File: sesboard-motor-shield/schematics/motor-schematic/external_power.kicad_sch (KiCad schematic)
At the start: 9 parts, among them J1 12Vin(MAX), Q1 Q_NMOS_DGS, Q2 TIP3055, U1 LM317_SOT-223

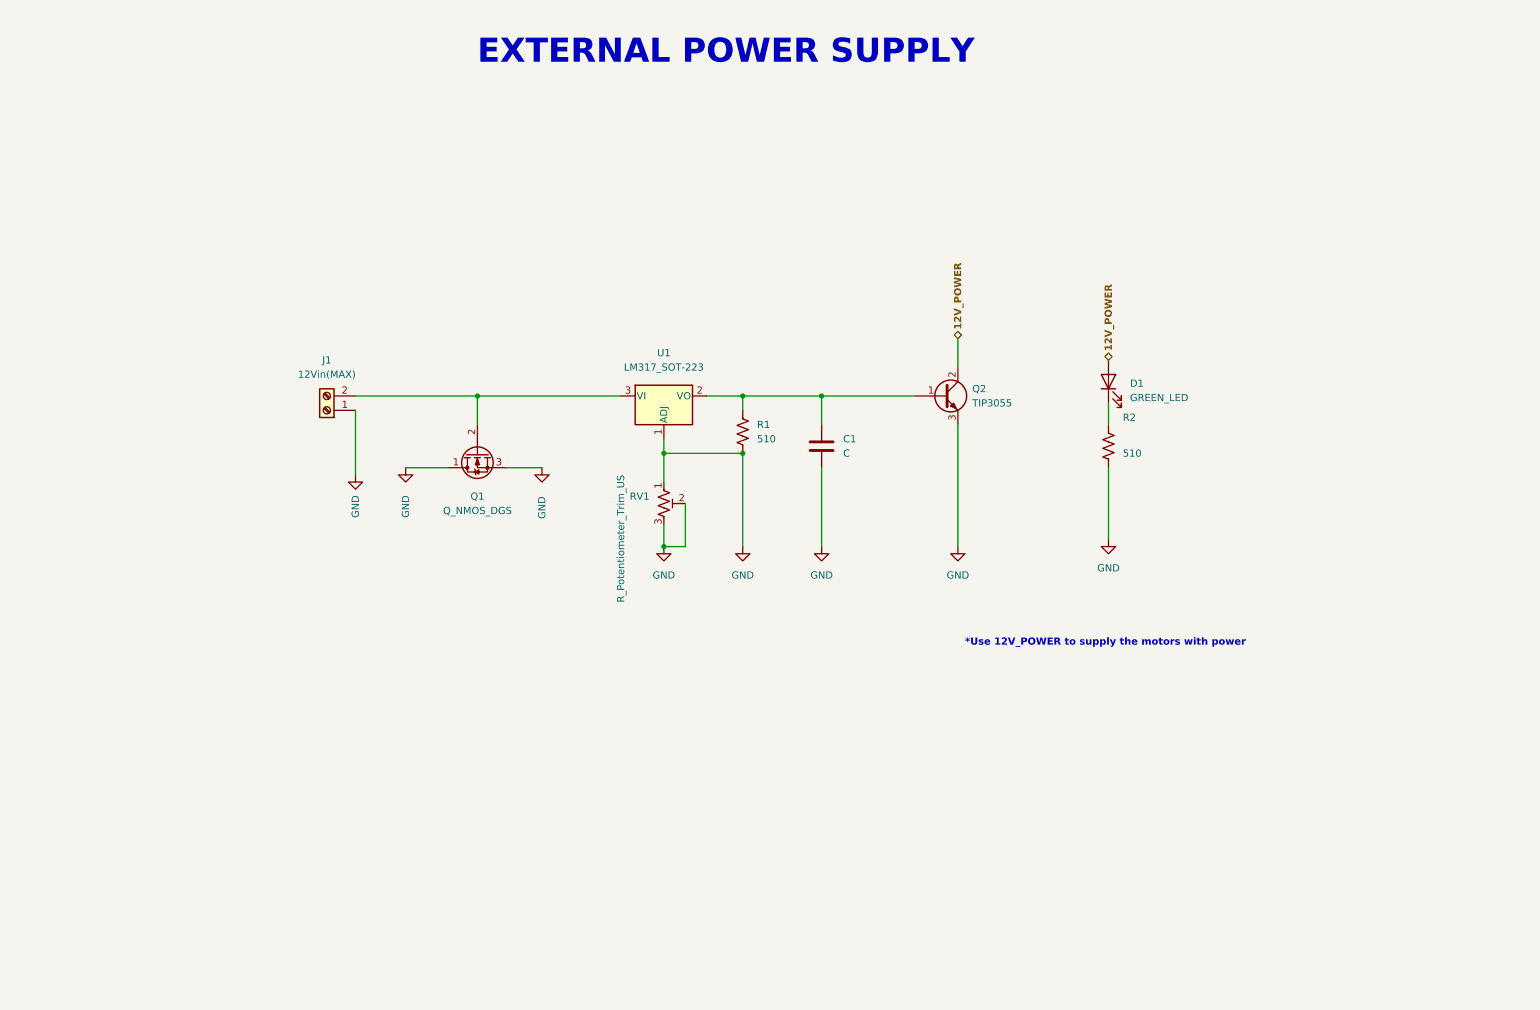
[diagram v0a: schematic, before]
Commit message: added servo power supply
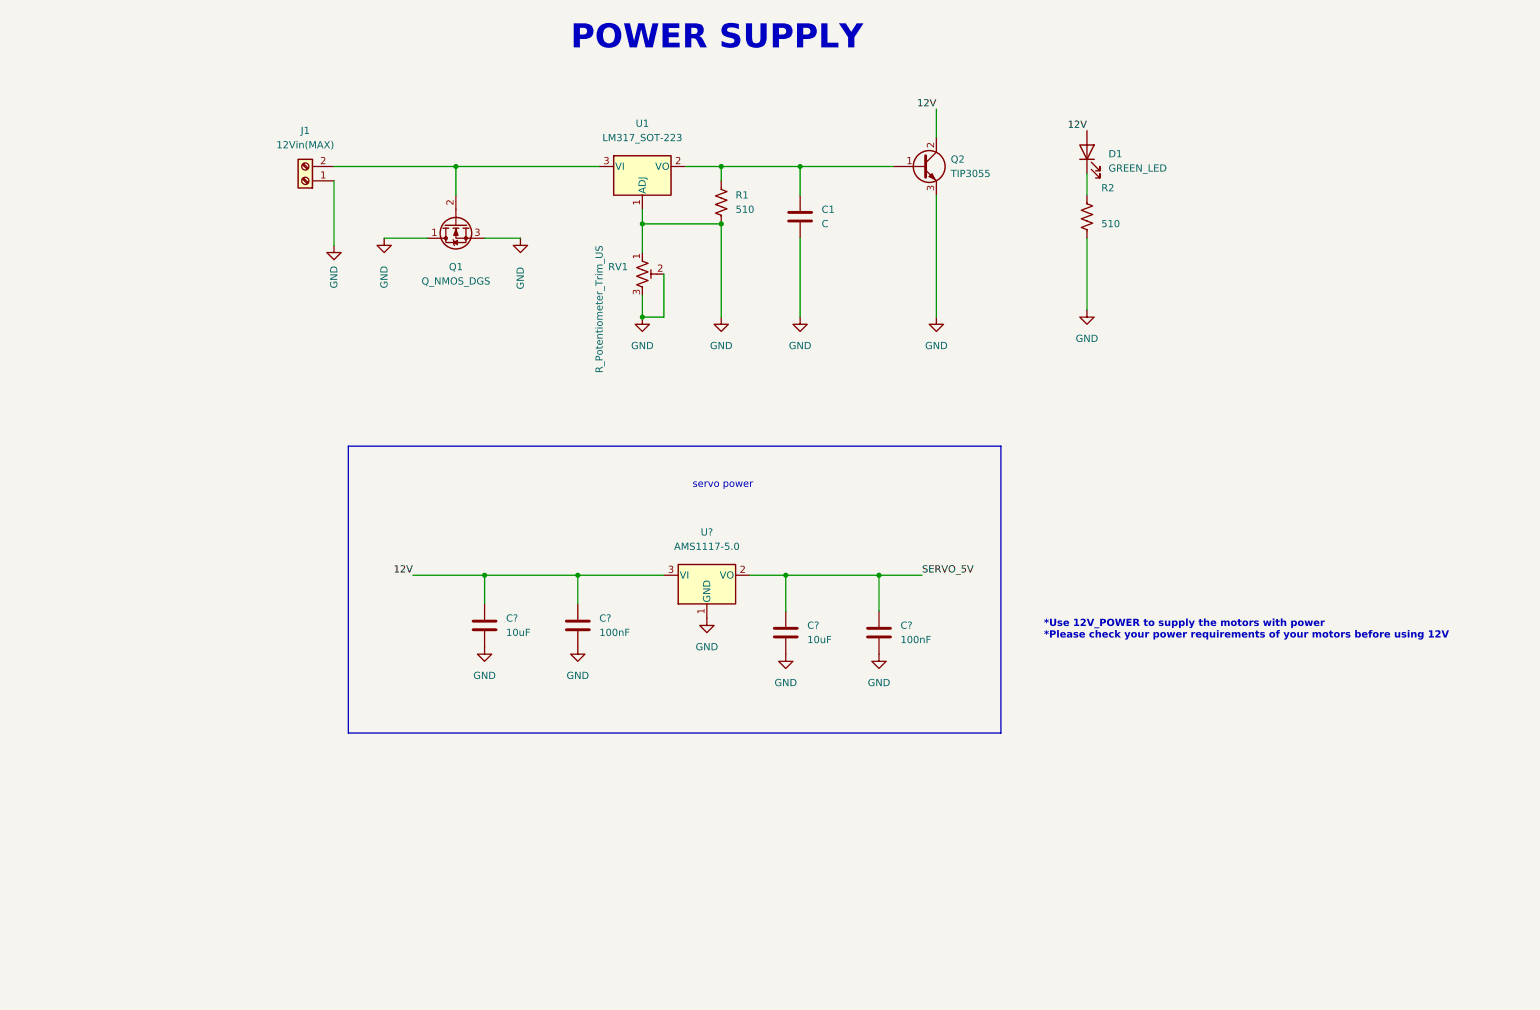
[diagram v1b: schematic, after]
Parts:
- added C? (x2): 10uF, symbol Device:C
- added C? (x2): 100nF, symbol Device:C
- added U?: AMS1117-5.0, Package_TO_SOT_SMD:SOT-223-3_TabPin2, symbol Regulator_Linear:AMS1117-5.0
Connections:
- net GND: now also C?.2, C?.2, C?.2, C?.2, U?.1 (GND)
- net 12V_POWER renamed 12V
- net 12V: now also C?.1, C?.1, U?.3 (VI)
- new net SERVO_5V: C?.1, C?.1, U?.2 (VO)
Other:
- note added: "*Use 12V_POWER to supply the motors with power *Please check your power requirements of your motors before using 12V"
- note added: "POWER SUPPLY"
- note added: "servo power"
- note removed: "*Use 12V_POWER to supply the motors with power"
- note removed: "EXTERNAL POWER SUPPLY"
- moved on the sheet: C1, D1, J1, Q1, Q2, R1, R2, RV1, U1

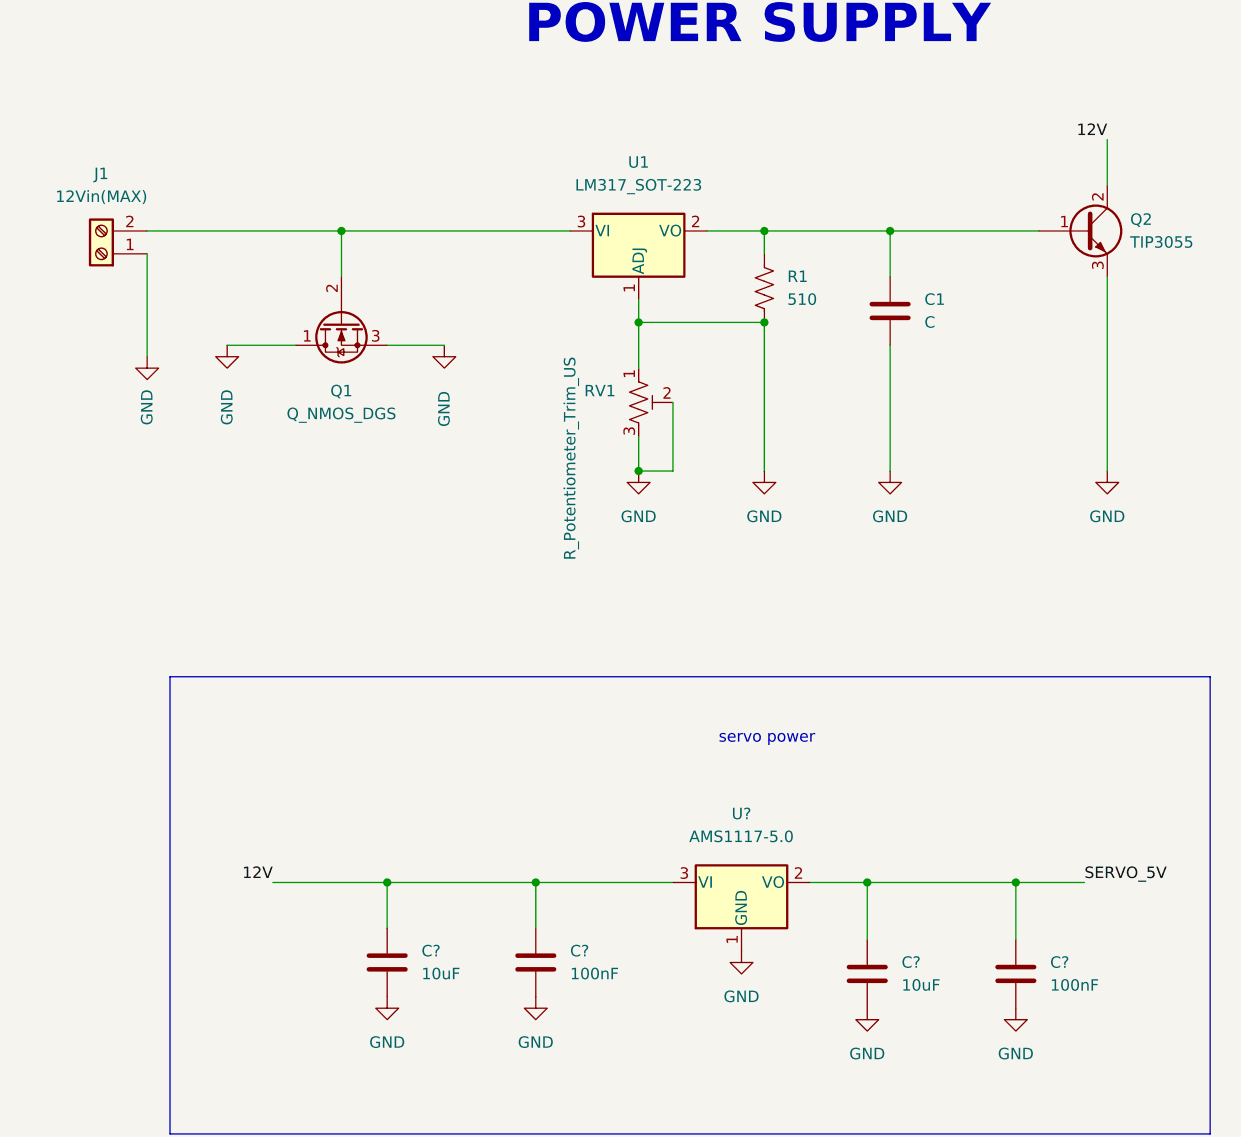
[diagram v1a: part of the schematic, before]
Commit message: performed ERC
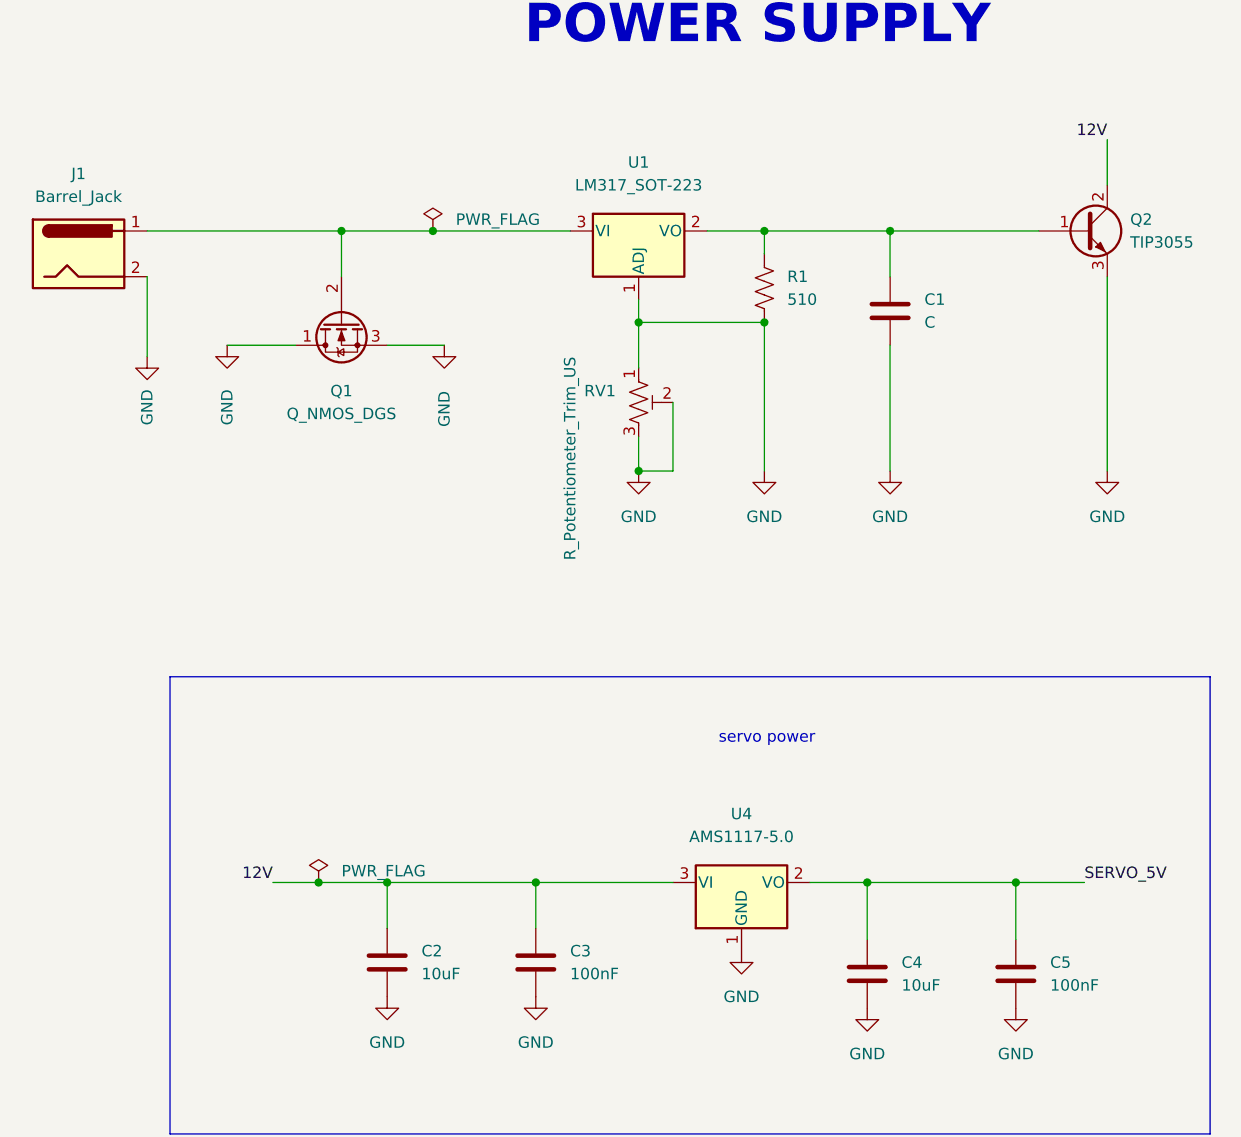
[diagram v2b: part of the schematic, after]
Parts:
- removed J1: 12Vin(MAX), symbol Connector:Screw_Terminal_01x02
- added J1: Barrel_Jack, symbol Connector:Barrel_Jack
- gave numbers to parts that had none: 5
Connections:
- net GND: now also J1.2
- net at Q1.2 (G), U1.3 (VI): now also J1.1
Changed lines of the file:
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@@
   (junction (at 160.02 41.91) (diameter 0) (color 0 0 0 0)
   )
+  (junction (at 96.52 114.3) (diameter 0) (color 0 0 0 0)
+  )
   (junction (at 99.06 41.91) (diameter 0) (color 0 0 0 0)
   )
   (junction (at 146.05 52.07) (diameter 0) (color 0 0 0 0)
   )
+  (junction (at 109.22 41.91) (diameter 0) (color 0 0 0 0)
+  )
   (junction (at 132.08 68.58) (diameter 0) (color 0 0 0 0)
   )
@@
     (stroke (width 0) (type default) (color 0 0 0 0))
   )
-  (wire (pts (xy 99.06 41.91) (xy 124.46 41.91))
+  (wire (pts (xy 99.06 41.91) (xy 109.22 41.91))
     (stroke (width 0) (type default) (color 0 0 0 0))
   )
@@
     (stroke (width 0) (type default) (color 0 0 0 0))
   )
-  (wire (pts (xy 77.47 55.88) (xy 77.47 44.45))
+  (wire (pts (xy 77.47 55.88) (xy 77.47 46.99))
     (stroke (width 0) (type default) (color 0 0 0 0))
   )
@@
     (stroke (width 0) (type default) (color 0 0 0 0))
   )
+  (wire (pts (xy 96.52 114.3) (xy 104.14 114.3))
+    (stroke (width 0) (type default) (color 0 0 0 0))
+  )
   (wire (pts (xy 146.05 41.91) (xy 139.7 41.91))
     (stroke (width 0) (type default) (color 0 0 0 0))
@@
     (stroke (width 0) (type default) (color 0 0 0 0))
   )
+  (wire (pts (xy 109.22 41.91) (xy 124.46 41.91))
+    (stroke (width 0) (type default) (color 0 0 0 0))
+  )
   (wire (pts (xy 210.82 43.18) (xy 210.82 46.99))
     (stroke (width 0) (type default) (color 0 0 0 0))
@@
     (stroke (width 0) (type default) (color 0 0 0 0))
   )
-  (wire (pts (xy 91.44 114.3) (xy 104.14 114.3))
+  (wire (pts (xy 91.44 114.3) (xy 96.52 114.3))
     (stroke (width 0) (type default) (color 0 0 0 0))
   )
@@
     (pin "2")
   )
+  (symbol (lib_id "power:PWR_FLAG") (at 109.22 41.91 0) (unit 1)
+    (in_bom yes) (on_board yes) (fields_autoplaced)
+    (property "Reference" "#FLG0101" (id 0) (at 109.22 40.005 0)
+      (effects (font (size 1.27 1.27)) hide)
+    )
+    (property "Value" "PWR_FLAG" (id 1) (at 111.76 40.6399 0)
+      (effects (font (size 1.27 1.27)) (justify left))
+    )
+    (property "Footprint" "" (id 2) (at 109.22 41.91 0)
+      (effects (font (size 1.27 1.27)) hide)
+    )
+    (property "Datasheet" "~" (id 3) (at 109.22 41.91 0)
+      (effects (font (size 1.27 1.27)) hide)
+    )
+    (pin "1")
+  )
   (symbol (lib_id "Device:C") (at 157.48 124.46 0) (unit 1)
     (in_bom yes) (on_board yes) (fields_autoplaced)
-    (property "Reference" "C?" (id 0) (at 161.29 123.1899 0)
+    (property "Reference" "C4" (id 0) (at 161.29 123.1899 0)
       (effects (font (size 1.27 1.27)) (justify left))
     )
@@
   (symbol (lib_id "Device:C") (at 173.99 124.46 0) (unit 1)
     (in_bom yes) (on_board yes)
-    (property "Reference" "C?" (id 0) (at 177.8 123.1899 0)
+    (property "Reference" "C5" (id 0) (at 177.8 123.1899 0)
       (effects (font (size 1.27 1.27)) (justify left))
     )
@@
   (symbol (lib_id "Regulator_Linear:AMS1117-5.0") (at 143.51 114.3 0) (unit 1)
     (in_bom yes) (on_board yes) (fields_autoplaced)
-    (property "Reference" "U?" (id 0) (at 143.51 106.68 0))
+    (property "Reference" "U4" (id 0) (at 143.51 106.68 0))
     (property "Value" "AMS1117-5.0" (id 1) (at 143.51 109.22 0))
     (property "Footprint" "Package_TO_SOT_SMD:SOT-223-3_TabPin2" (id 2) (at 143.51 109.22 0)
@@
     (pin "1")
   )
-  (symbol (lib_id "Connector:Screw_Terminal_01x02") (at 72.39 44.45 180) (unit 1)
-    (in_bom yes) (on_board yes) (fields_autoplaced)
-    (property "Reference" "J1" (id 0) (at 72.39 35.56 0))
-    (property "Value" "12Vin(MAX)" (id 1) (at 72.39 38.1 0))
-    (property "Footprint" "" (id 2) (at 72.39 44.45 0)
-      (effects (font (size 1.27 1.27)) hide)
-    )
-    (property "Datasheet" "~" (id 3) (at 72.39 44.45 0)
+  (symbol (lib_id "power:PWR_FLAG") (at 96.52 114.3 0) (unit 1)
+    (in_bom yes) (on_board yes) (fields_autoplaced)
+    (property "Reference" "#FLG0102" (id 0) (at 96.52 112.395 0)
+      (effects (font (size 1.27 1.27)) hide)
+    )
+    (property "Value" "PWR_FLAG" (id 1) (at 99.06 113.0299 0)
+      (effects (font (size 1.27 1.27)) (justify left))
+    )
+    (property "Footprint" "" (id 2) (at 96.52 114.3 0)
+      (effects (font (size 1.27 1.27)) hide)
+    )
+    (property "Datasheet" "~" (id 3) (at 96.52 114.3 0)
+      (effects (font (size 1.27 1.27)) hide)
+    )
+    (pin "1")
+  )
+  (symbol (lib_id "Connector:Barrel_Jack") (at 69.85 44.45 0) (unit 1)
+    (in_bom yes) (on_board yes) (fields_autoplaced)
+    (property "Reference" "J1" (id 0) (at 69.85 35.56 0))
+    (property "Value" "Barrel_Jack" (id 1) (at 69.85 38.1 0))
+    (property "Footprint" "" (id 2) (at 71.12 45.466 0)
+      (effects (font (size 1.27 1.27)) hide)
+    )
+    (property "Datasheet" "~" (id 3) (at 71.12 45.466 0)
       (effects (font (size 1.27 1.27)) hide)
     )
@@
   (symbol (lib_id "Device:C") (at 104.14 123.19 0) (unit 1)
     (in_bom yes) (on_board yes) (fields_autoplaced)
-    (property "Reference" "C?" (id 0) (at 107.95 121.9199 0)
+    (property "Reference" "C2" (id 0) (at 107.95 121.9199 0)
       (effects (font (size 1.27 1.27)) (justify left))
     )
@@
   (symbol (lib_id "power:GND") (at 173.99 128.27 0) (unit 1)
     (in_bom yes) (on_board yes) (fields_autoplaced)
-    (property "Reference" "#PWR?" (id 0) (at 173.99 134.62 0)
+    (property "Reference" "#PWR020" (id 0) (at 173.99 134.62 0)
       (effects (font (size 1.27 1.27)) hide)
     )
@@
   (symbol (lib_id "power:GND") (at 143.51 121.92 0) (unit 1)
     (in_bom yes) (on_board yes) (fields_autoplaced)
-    (property "Reference" "#PWR?" (id 0) (at 143.51 128.27 0)
+    (property "Reference" "#PWR018" (id 0) (at 143.51 128.27 0)
       (effects (font (size 1.27 1.27)) hide)
     )
@@
   (symbol (lib_id "power:GND") (at 157.48 128.27 0) (unit 1)
     (in_bom yes) (on_board yes) (fields_autoplaced)
-    (property "Reference" "#PWR?" (id 0) (at 157.48 134.62 0)
+    (property "Reference" "#PWR019" (id 0) (at 157.48 134.62 0)
       (effects (font (size 1.27 1.27)) hide)
     )
@@
   (symbol (lib_id "power:GND") (at 120.65 127 0) (unit 1)
     (in_bom yes) (on_board yes) (fields_autoplaced)
-    (property "Reference" "#PWR?" (id 0) (at 120.65 133.35 0)
+    (property "Reference" "#PWR017" (id 0) (at 120.65 133.35 0)
       (effects (font (size 1.27 1.27)) hide)
     )
@@
   (symbol (lib_id "power:GND") (at 104.14 127 0) (unit 1)
     (in_bom yes) (on_board yes) (fields_autoplaced)
-    (property "Reference" "#PWR?" (id 0) (at 104.14 133.35 0)
+    (property "Reference" "#PWR016" (id 0) (at 104.14 133.35 0)
       (effects (font (size 1.27 1.27)) hide)
     )
@@
   (symbol (lib_id "Device:C") (at 120.65 123.19 0) (unit 1)
     (in_bom yes) (on_board yes) (fields_autoplaced)
-    (property "Reference" "C?" (id 0) (at 124.46 121.9199 0)
-      (effects (font (size 1.27 1.27)) (justify left))
-    )
+    (property "Reference" "C3" (id 0) (at 124.46 121.9199 0)
+      (effects (font (size 1.27 1.27)) (justify left))
+    )
